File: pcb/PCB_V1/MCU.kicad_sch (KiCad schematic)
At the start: 19 parts, among them J201 UART / 3V3 logic, SW201 RESET, SW202 BOOT, U201 ESP32-WROOM-32E-N4

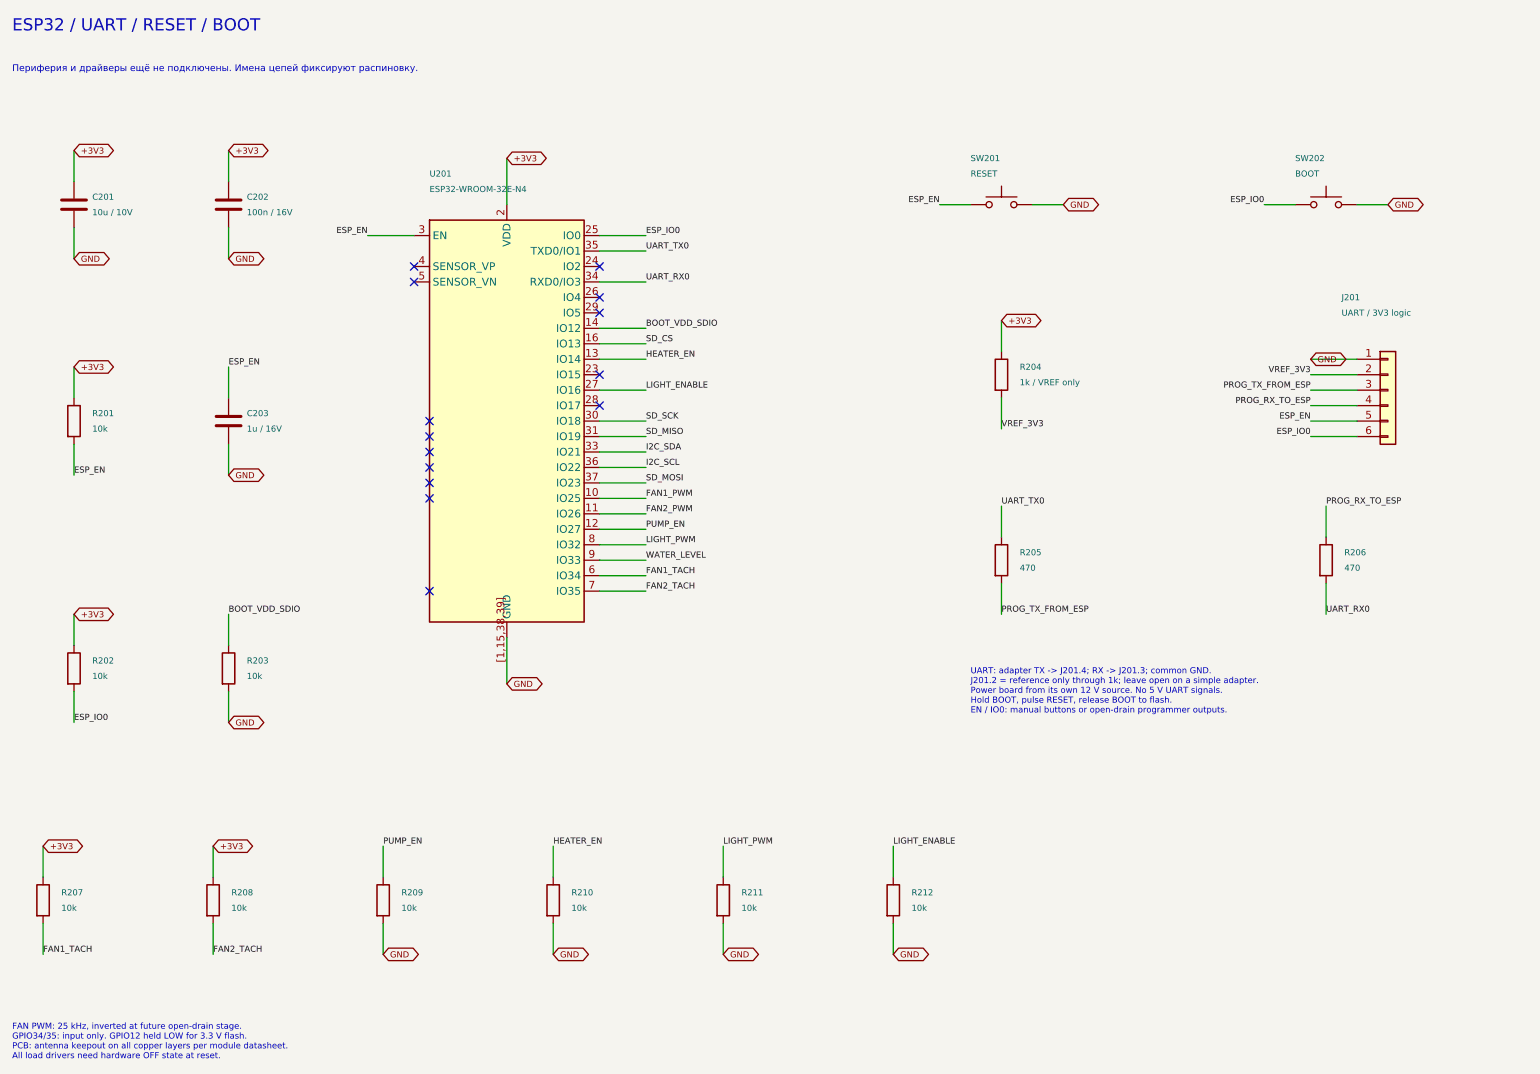
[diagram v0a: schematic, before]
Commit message: Add RTC, microSD and protected sensor interfaces to PCB schematic
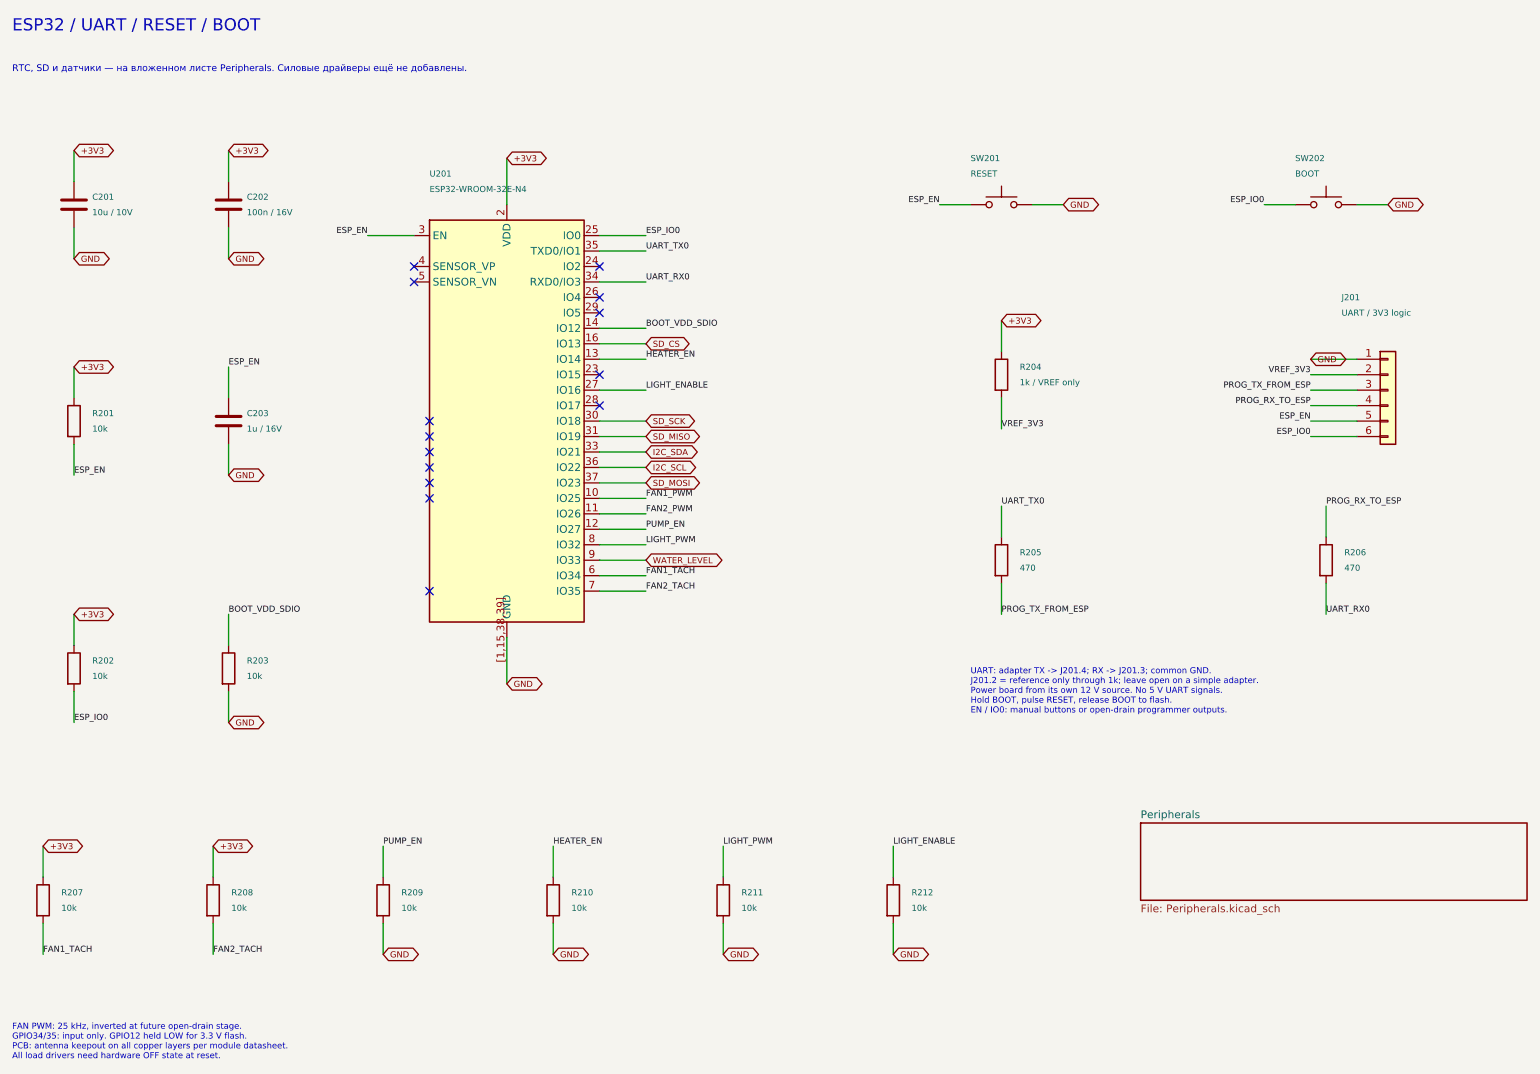
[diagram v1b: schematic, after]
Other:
- added sheet Peripherals (Peripherals.kicad_sch)
- note added: "RTC, SD и датчики — на вложенном листе Peripherals. Силовые драйверы ещё не добавлены."
- note removed: "Периферия и драйверы ещё не подключены. Имена цепей фиксируют распиновку."

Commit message: pcb: add fan pump and PTC output stages
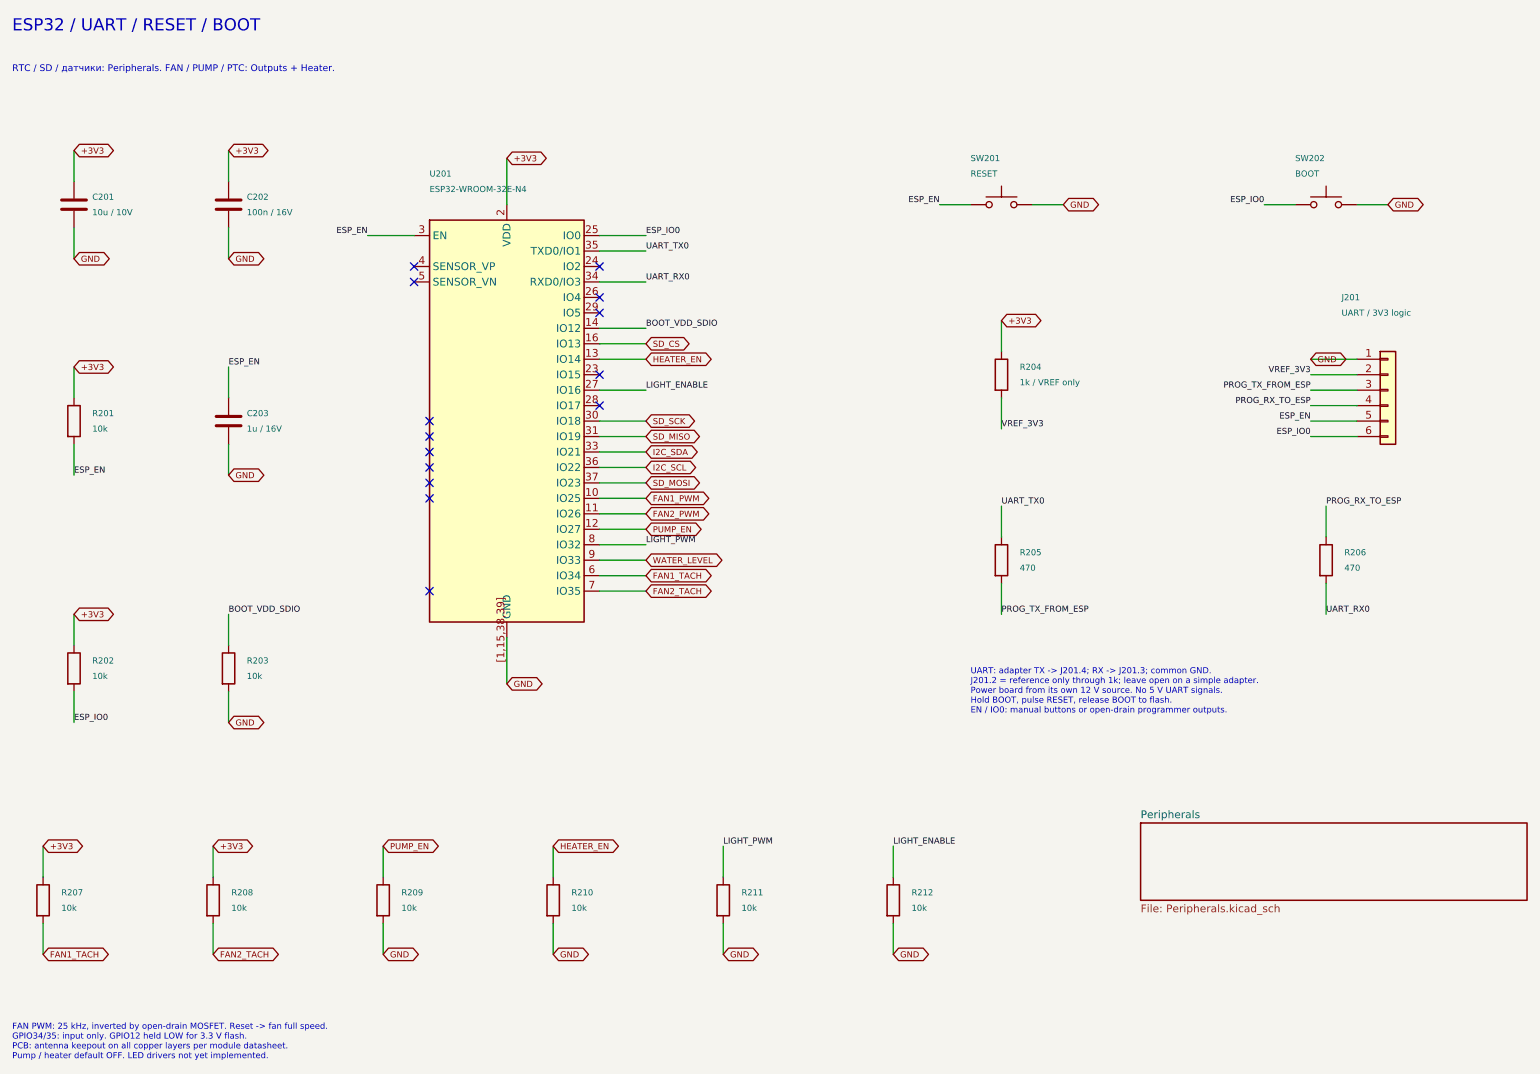
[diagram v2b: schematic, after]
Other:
- note added: "FAN PWM: 25 kHz, inverted by open-drain MOSFET. Reset -> fan full speed. GPIO34/35: input only. GPIO12 held LOW for 3.3 V flash. PCB: antenna keepout on all copper layers per module datasheet. Pump / heater default OFF. LED drivers not yet implemented."
- note added: "RTC / SD / датчики: Peripherals. FAN / PUMP / PTC: Outputs + Heater."
- note removed: "FAN PWM: 25 kHz, inverted at future open-drain stage. GPIO34/35: input only. GPIO12 held LOW for 3.3 V flash. PCB: antenna keepout on all copper layers per module datasheet. All load drivers need hardware OFF state at reset."
- note removed: "RTC, SD и датчики — на вложенном листе Peripherals. Силовые драйверы ещё не добавлены."
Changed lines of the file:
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@@
 		(title "02 - ESP32 and programming")
 		(date "2026-09-26")
-		(rev "0.2-DRAFT")
+		(rev "0.3-DRAFT")
 		(company "GrowBox controller")
-		(comment 1 "Logic first; power loads not yet implemented")
+		(comment 1 "Draft: input protection and LED drivers pending")
 	)
 	(text "UART: adapter TX -> J201.4; RX -> J201.3; common GND.\nJ201.2 = reference only through 1k; leave open on a simple adapter.\nPower board from its own 12 V source. No 5 V UART signals.\nHold BOOT, pulse RESET, release BOOT to flash.\nEN / IO0: manual buttons or open-drain programmer outputs."
@@
 		)
 	)
-	(text "RTC, SD и датчики — на вложенном листе Peripherals. Силовые драйверы ещё не добавлены."
+	(text "RTC / SD / датчики: Peripherals. FAN / PUMP / PTC: Outputs + Heater."
 		(exclude_from_sim no)
 		(at 20.32 22.86 0)
@@
 		)
 	)
-	(text "FAN PWM: 25 kHz, inverted at future open-drain stage.\nGPIO34/35: input only. GPIO12 held LOW for 3.3 V flash.\nPCB: antenna keepout on all copper layers per module datasheet.\nAll load drivers need hardware OFF state at reset."
+	(text "FAN PWM: 25 kHz, inverted by open-drain MOSFET. Reset -> fan full speed.\nGPIO34/35: input only. GPIO12 held LOW for 3.3 V flash.\nPCB: antenna keepout on all copper layers per module datasheet.\nPump / heater default OFF. LED drivers not yet implemented."
 		(exclude_from_sim no)
 		(at 20.32 180.34 0)
@@
 		)
 	)
-	(label "HEATER_EN"
-		(at 109.22 151.13 0)
-		(effects
-			(font
-				(size 1 1)
-			)
-			(justify left bottom)
-		)
-	)
 	(label "ESP_EN"
 		(at 172.72 45.72 180)
@@
 		)
 	)
-	(label "FAN1_TACH"
-		(at 25.4 168.91 0)
-		(effects
-			(font
-				(size 1 1)
-			)
-			(justify left bottom)
-		)
-	)
-	(label "FAN1_TACH"
-		(at 124.46 106.68 0)
-		(effects
-			(font
-				(size 1 1)
-			)
-			(justify left bottom)
-		)
-	)
 	(label "LIGHT_PWM"
 		(at 124.46 101.6 0)
@@
 		)
 	)
-	(label "FAN2_PWM"
-		(at 124.46 96.52 0)
-		(effects
-			(font
-				(size 1 1)
-			)
-			(justify left bottom)
-		)
-	)
-	(label "FAN1_PWM"
-		(at 124.46 93.98 0)
-		(effects
-			(font
-				(size 1 1)
-			)
-			(justify left bottom)
-		)
-	)
 	(label "VREF_3V3"
 		(at 233.68 73.66 180)
@@
 		)
 	)
-	(label "FAN2_TACH"
-		(at 124.46 109.22 0)
-		(effects
-			(font
-				(size 1 1)
-			)
-			(justify left bottom)
-		)
-	)
-	(label "HEATER_EN"
-		(at 124.46 71.12 0)
-		(effects
-			(font
-				(size 1 1)
-			)
-			(justify left bottom)
-		)
-	)
 	(label "ESP_IO0"
 		(at 226.06 45.72 180)
@@
 		)
 	)
-	(label "FAN2_TACH"
-		(at 53.34 168.91 0)
-		(effects
-			(font
-				(size 1 1)
-			)
-			(justify left bottom)
-		)
-	)
 	(label "ESP_IO0"
 		(at 233.68 83.82 180)
@@
 		)
 	)
-	(label "PUMP_EN"
-		(at 124.46 99.06 0)
-		(effects
-			(font
-				(size 1 1)
-			)
-			(justify left bottom)
-		)
-	)
 	(label "LIGHT_ENABLE"
 		(at 165.1 151.13 0)
@@
 		)
 	)
-	(label "PUMP_EN"
-		(at 81.28 151.13 0)
-		(effects
-			(font
-				(size 1 1)
-			)
-			(justify left bottom)
-		)
-	)
 	(label "PROG_RX_TO_ESP"
 		(at 236.22 95.25 0)
@@
 		)
 	)
+	(global_label "HEATER_EN"
+		(shape bidirectional)
+		(at 109.22 151.13 0)
+		(effects
+			(font
+				(size 1 1)
+			)
+			(justify left bottom)
+		)
+		(property "Intersheetrefs" "${INTERSHEET_REFS}"
+			(at 109.22 151.13 0)
+			(hide yes)
+			(show_name no)
+			(do_not_autoplace no)
+			(effects
+				(font
+					(size 1.27 1.27)
+				)
+			)
+		)
+	)
 	(global_label "GND"
 		(shape bidirectional)
@@
 		)
 	)
+	(global_label "FAN1_TACH"
+		(shape bidirectional)
+		(at 25.4 168.91 0)
+		(effects
+			(font
+				(size 1 1)
+			)
+			(justify left bottom)
+		)
+		(property "Intersheetrefs" "${INTERSHEET_REFS}"
+			(at 25.4 168.91 0)
+			(hide yes)
+			(show_name no)
+			(do_not_autoplace no)
+			(effects
+				(font
+					(size 1.27 1.27)
+				)
+			)
+		)
+	)
 	(global_label "GND"
 		(shape bidirectional)
@@
 		)
 	)
+	(global_label "FAN1_TACH"
+		(shape bidirectional)
+		(at 124.46 106.68 0)
+		(effects
+			(font
+				(size 1 1)
+			)
+			(justify left bottom)
+		)
+		(property "Intersheetrefs" "${INTERSHEET_REFS}"
+			(at 124.46 106.68 0)
+			(hide yes)
+			(show_name no)
+			(do_not_autoplace no)
+			(effects
+				(font
+					(size 1.27 1.27)
+				)
+			)
+		)
+	)
+	(global_label "FAN2_PWM"
+		(shape bidirectional)
+		(at 124.46 96.52 0)
+		(effects
+			(font
+				(size 1 1)
+			)
+			(justify left bottom)
+		)
+		(property "Intersheetrefs" "${INTERSHEET_REFS}"
+			(at 124.46 96.52 0)
+			(hide yes)
+			(show_name no)
+			(do_not_autoplace no)
+			(effects
+				(font
+					(size 1.27 1.27)
+				)
+			)
+		)
+	)
+	(global_label "FAN1_PWM"
+		(shape bidirectional)
+		(at 124.46 93.98 0)
+		(effects
+			(font
+				(size 1 1)
+			)
+			(justify left bottom)
+		)
+		(property "Intersheetrefs" "${INTERSHEET_REFS}"
+			(at 124.46 93.98 0)
+			(hide yes)
+			(show_name no)
+			(do_not_autoplace no)
+			(effects
+				(font
+					(size 1.27 1.27)
+				)
+			)
+		)
+	)
 	(global_label "GND"
 		(shape bidirectional)
@@
 		)
 	)
+	(global_label "FAN2_TACH"
+		(shape bidirectional)
+		(at 124.46 109.22 0)
+		(effects
+			(font
+				(size 1 1)
+			)
+			(justify left bottom)
+		)
+		(property "Intersheetrefs" "${INTERSHEET_REFS}"
+			(at 124.46 109.22 0)
+			(hide yes)
+			(show_name no)
+			(do_not_autoplace no)
+			(effects
+				(font
+					(size 1.27 1.27)
+				)
+			)
+		)
+	)
+	(global_label "HEATER_EN"
+		(shape bidirectional)
+		(at 124.46 71.12 0)
+		(effects
+			(font
+				(size 1 1)
+			)
+			(justify left bottom)
+		)
+		(property "Intersheetrefs" "${INTERSHEET_REFS}"
+			(at 124.46 71.12 0)
+			(hide yes)
+			(show_name no)
+			(do_not_autoplace no)
+			(effects
+				(font
+					(size 1.27 1.27)
+				)
+			)
+		)
+	)
 	(global_label "GND"
 		(shape bidirectional)
@@
 		)
 	)
+	(global_label "FAN2_TACH"
+		(shape bidirectional)
+		(at 53.34 168.91 0)
+		(effects
+			(font
+				(size 1 1)
+			)
+			(justify left bottom)
+		)
+		(property "Intersheetrefs" "${INTERSHEET_REFS}"
+			(at 53.34 168.91 0)
+			(hide yes)
+			(show_name no)
+			(do_not_autoplace no)
+			(effects
+				(font
+					(size 1.27 1.27)
+				)
+			)
+		)
+	)
 	(global_label "+3V3"
 		(shape bidirectional)
@@
 		)
 	)
+	(global_label "PUMP_EN"
+		(shape bidirectional)
+		(at 124.46 99.06 0)
+		(effects
+			(font
+				(size 1 1)
+			)
+			(justify left bottom)
+		)
+		(property "Intersheetrefs" "${INTERSHEET_REFS}"
+			(at 124.46 99.06 0)
+			(hide yes)
+			(show_name no)
+			(do_not_autoplace no)
+			(effects
+				(font
+					(size 1.27 1.27)
+				)
+			)
+		)
+	)
 	(global_label "SD_CS"
 		(shape bidirectional)
@@
 			(hide yes)
 			(show_name no)
+			(do_not_autoplace no)
+			(effects
+				(font
+					(size 1.27 1.27)
+				)
+			)
+		)
+	)
+	(global_label "PUMP_EN"
+		(shape bidirectional)
+		(at 81.28 151.13 0)
+		(effects
+			(font
+				(size 1 1)
+			)
+			(justify left bottom)
+		)
+		(property "Intersheetrefs" "${INTERSHEET_REFS}"
+			(at 81.28 151.13 0)
+			(hide yes)
+			(show_name no)

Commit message: pcb: add protected input and independent LED boost drivers
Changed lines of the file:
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@@
 		(title "02 - ESP32 and programming")
 		(date "2026-09-26")
-		(rev "0.3-DRAFT")
+		(rev "0.4-DRAFT")
 		(company "GrowBox controller")
 		(comment 1 "Draft: input protection and LED drivers pending")
@@
 		)
 	)
-	(label "LIGHT_PWM"
-		(at 124.46 101.6 0)
-		(effects
-			(font
-				(size 1 1)
-			)
-			(justify left bottom)
-		)
-	)
 	(label "BOOT_VDD_SDIO"
 		(at 55.88 113.03 0)
@@
 		)
 	)
-	(label "LIGHT_PWM"
-		(at 137.16 151.13 0)
-		(effects
-			(font
-				(size 1 1)
-			)
-			(justify left bottom)
-		)
-	)
 	(label "ESP_EN"
 		(at 30.48 90.17 0)
@@
 		)
 	)
-	(label "LIGHT_ENABLE"
-		(at 124.46 76.2 0)
-		(effects
-			(font
-				(size 1 1)
-			)
-			(justify left bottom)
-		)
-	)
 	(label "PROG_TX_FROM_ESP"
 		(at 233.68 76.2 180)
@@
 		)
 	)
-	(label "LIGHT_ENABLE"
-		(at 165.1 151.13 0)
-		(effects
-			(font
-				(size 1 1)
-			)
-			(justify left bottom)
-		)
-	)
 	(label "PROG_RX_TO_ESP"
 		(at 236.22 95.25 0)
@@
 		)
 	)
+	(global_label "LIGHT_PWM"
+		(shape bidirectional)
+		(at 124.46 101.6 0)
+		(effects
+			(font
+				(size 1 1)
+			)
+			(justify left bottom)
+		)
+		(property "Intersheetrefs" "${INTERSHEET_REFS}"
+			(at 124.46 101.6 0)
+			(hide yes)
+			(show_name no)
+			(do_not_autoplace no)
+			(effects
+				(font
+					(size 1.27 1.27)
+				)
+			)
+		)
+	)
 	(global_label "FAN2_PWM"
 		(shape bidirectional)
@@
 		)
 	)
+	(global_label "LIGHT_PWM"
+		(shape bidirectional)
+		(at 137.16 151.13 0)
+		(effects
+			(font
+				(size 1 1)
+			)
+			(justify left bottom)
+		)
+		(property "Intersheetrefs" "${INTERSHEET_REFS}"
+			(at 137.16 151.13 0)
+			(hide yes)
+			(show_name no)
+			(do_not_autoplace no)
+			(effects
+				(font
+					(size 1.27 1.27)
+				)
+			)
+		)
+	)
 	(global_label "GND"
 		(shape bidirectional)
@@
 		)
 	)
+	(global_label "LIGHT_ENABLE"
+		(shape bidirectional)
+		(at 124.46 76.2 0)
+		(effects
+			(font
+				(size 1 1)
+			)
+			(justify left bottom)
+		)
+		(property "Intersheetrefs" "${INTERSHEET_REFS}"
+			(at 124.46 76.2 0)
+			(hide yes)
+			(show_name no)
+			(do_not_autoplace no)
+			(effects
+				(font
+					(size 1.27 1.27)
+				)
+			)
+		)
+	)
 	(global_label "I2C_SDA"
 		(shape bidirectional)
@@
 			(hide yes)
 			(show_name no)
+			(do_not_autoplace no)
+			(effects
+				(font
+					(size 1.27 1.27)
+				)
+			)
+		)
+	)
+	(global_label "LIGHT_ENABLE"
+		(shape bidirectional)
+		(at 165.1 151.13 0)
+		(effects
+			(font
+				(size 1 1)
+			)
+			(justify left bottom)
+		)
+		(property "Intersheetrefs" "${INTERSHEET_REFS}"
+			(at 165.1 151.13 0)
+			(hide yes)
+			(show_name no)
